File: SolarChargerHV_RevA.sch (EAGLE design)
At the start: 134 parts, among them CON1 CON_4X200MIL, CON2 USB_BMULTICOMP, CON3 ICSP, CON4 CON_3X100MIL, CON5 CON_3X100MIL, CON6 CON_8X200MIL, CON7 CON_2X100MIL, IC1 MCP3428, IC10 AT45DB161E, IC12 MCP14A0153, IC13 MCP14A0153, IC2 LMR62014, IC3 MIC4605-1YM, IC4 MCP1755, IC5 PIC18F46J50, IC6 TS6001, IC7 LMT86, IC8 24AA16, Q10 NTR4101PT1G, Q11 N-FET, Q12 N-FET, Q13 N-FET, Q14 N-FET, Q15 NX3008NBKW, Q2 PSMN6R0-30YL, Q3 NX3008NBKW, Q4 NTR4101PT1G, Q5 IPB039N10N3, Q6 IPB039N10N3, Q9 NX3008NBKW, X1 ABS07-120-32.768KHZ-T, X2 ABM3-8.000MHZ-D2Y-T, X3 USB_A, X4 USB_A

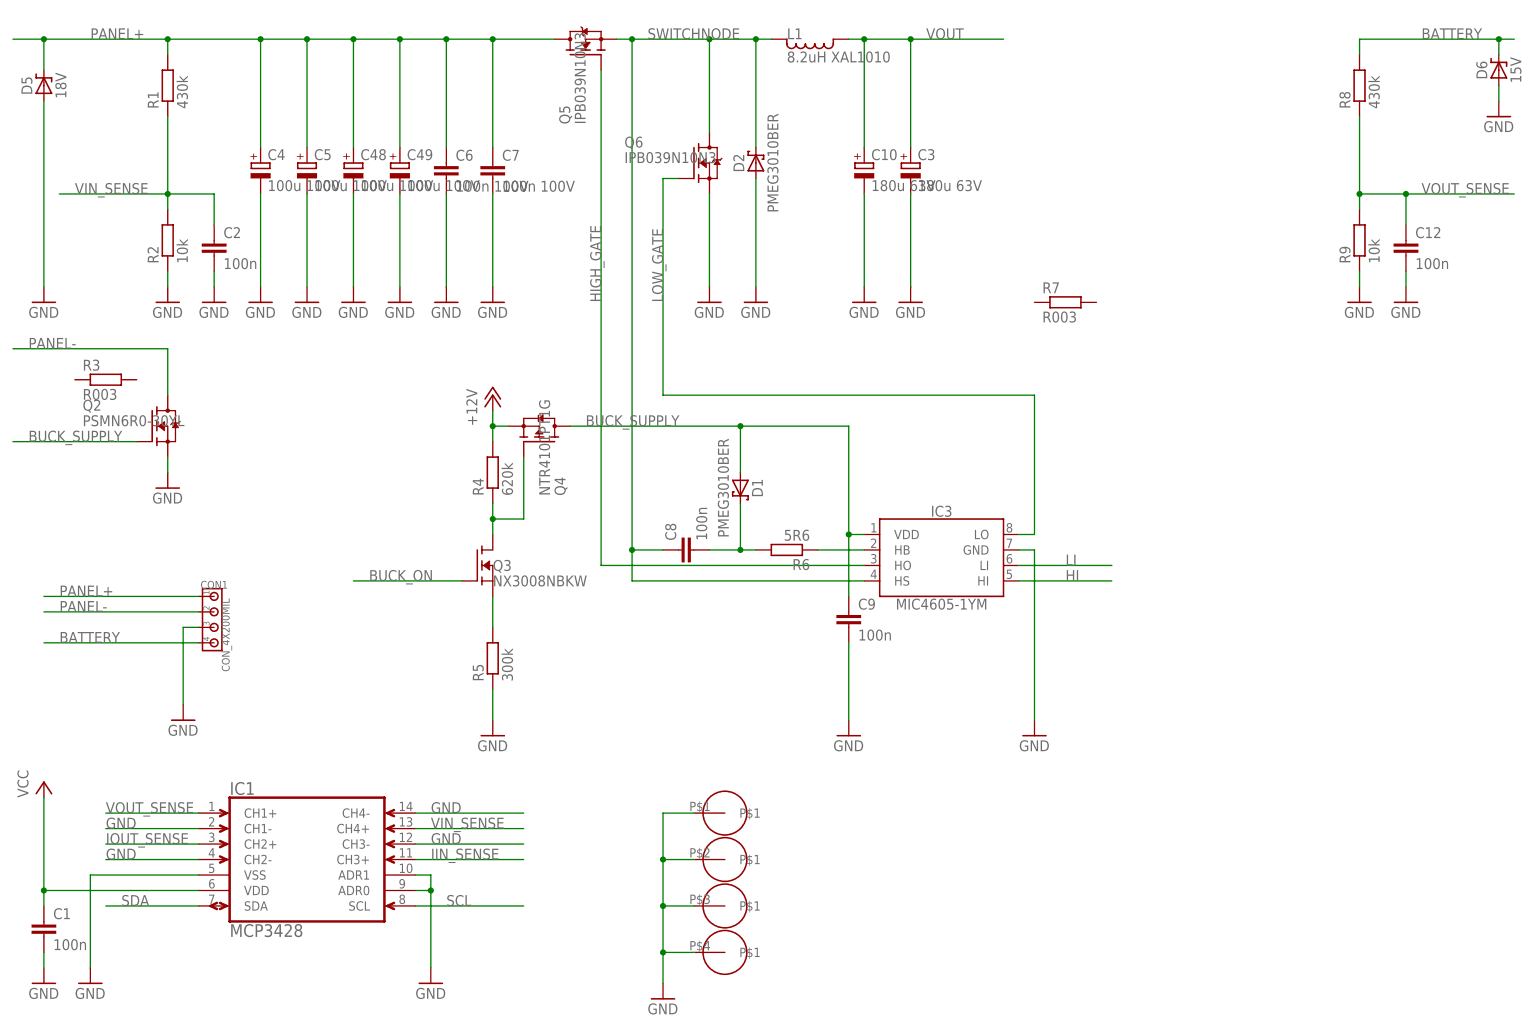
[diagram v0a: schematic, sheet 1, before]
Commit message: Buck for high voltage version nearly completed. Mosfet footprint still to be changed. Low-side current sensing implemented
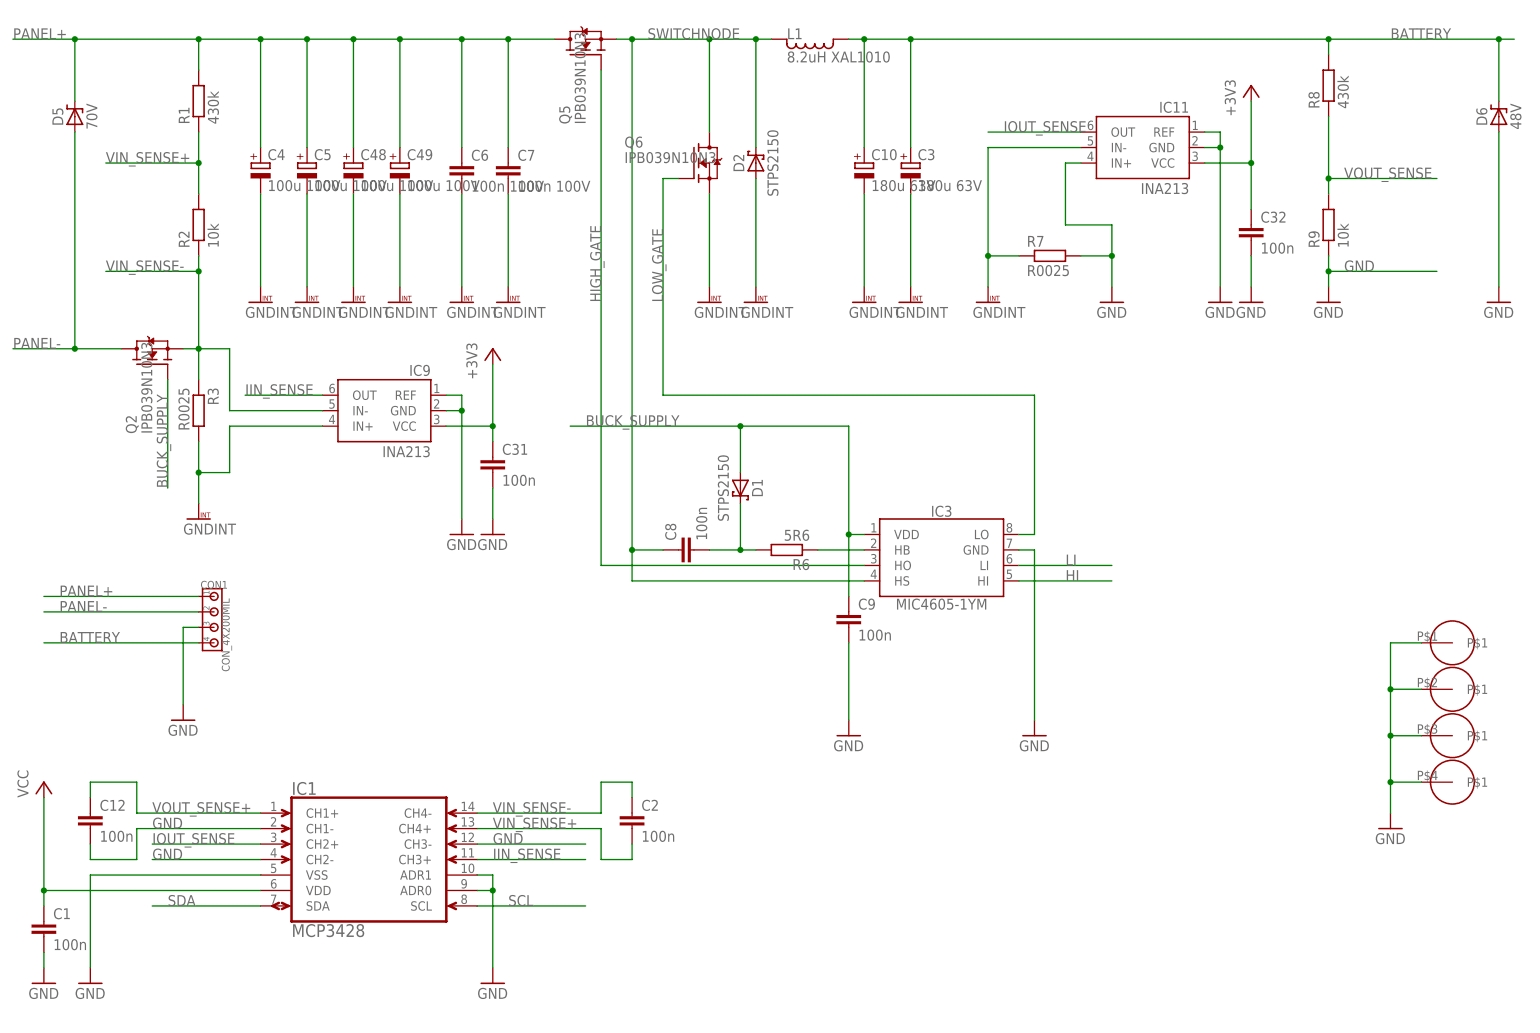
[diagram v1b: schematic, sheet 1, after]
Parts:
- removed Q3: NX3008NBKW, 00Mosfet:N-FETSOT23
- removed Q4: NTR4101PT1G, 00Mosfet:P-FETSOT23
- removed R4: 620k, 00Resistor:RESISTORR0805
- removed R5: 300k, 00Resistor:RESISTORR0805
- added C31, C32: 100n, 00Capacitor:CC0805
- added IC11, IC9: INA213, 00Sensor:INA21
- D1, D2: value PMEG3010BER -> STPS2150; device 00Diode:SCHOTTKYSOD123 -> 00Diode:SCHOTTKYDO214AC
- D5: value 18V -> 70V
- D6: value 15V -> 48V
- Q2: value PSMN6R0-30YL -> IPB039N10N3
- R3, R7: value R003 -> R0025
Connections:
- removed net N$16: Q3.D, Q4.G, R4.1
- removed net N$19: Q3.S, R5.2
- removed net VIN_SENSE: C2.1, IC1.CH4+, R1.1, R2.2
- removed net VOUT: C10.+, C3.+, L1.1, Q4.S, R4.2
- new net GNDINT: C10.-, C3.-, C4.-, C48.-, C49.-, C5.-, C6.2, C7.2, D2.A, IC11.IN-, IC9.IN+, Q6.S, R3.2, R7.1
- new net VIN_SENSE+: C2.2, IC1.CH4+, R1.1, R2.2
- new net VIN_SENSE-: C2.1, IC1.CH4-, IC9.IN-, Q2.S, R2.1, R3.1
- new net VOUT_SENSE+: C12.1, IC1.CH1+
- net +3V3: now also C31.1, C32.1, IC11.VCC, IC9.VCC
- net BATTERY: now also C10.+, C3.+, L1.1
- net BUCK_ON: no longer Q3.G
- net BUCK_SUPPLY: no longer Q4.D
- net GND: now also C31.2, C32.2, IC11.GND, IC11.IN+, IC11.REF, IC9.GND, IC9.REF, R7.2; no longer C10.-, C2.2, C3.-, C4.-, C48.-, C49.-, C5.-, C6.2, C7.2, D2.A, D5.A, IC1.CH4-, Q2.S, Q6.S, R2.1, R5.1
- net IIN_SENSE: now also IC9.OUT
- net IOUT_SENSE: now also IC11.OUT
- net PANEL-: now also D5.A
- net VOUT_SENSE: no longer C12.1, IC1.CH1+
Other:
- moved on the sheet: C12, C2, C6, C7, D5, D6, IC1, Q2, R1, R2, R3, R7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

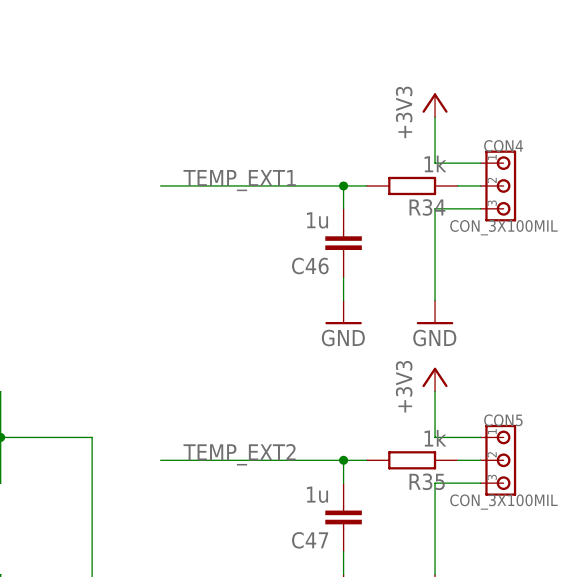
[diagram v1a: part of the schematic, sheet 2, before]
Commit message: Flash now supplied directly from VCC
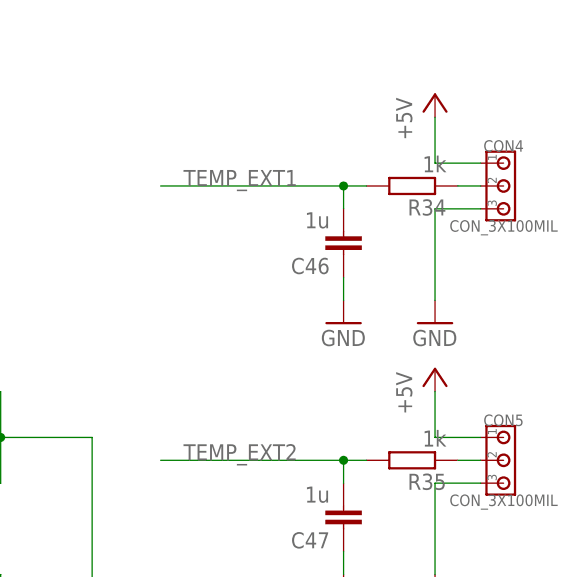
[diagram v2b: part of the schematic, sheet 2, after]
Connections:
- net +3V3: no longer CON4.1, CON5.1
- net +5V: now also CON4.1, CON5.1
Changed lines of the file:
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@@
 <part name="+3V2" library="00Supply" deviceset="+3V3" device=""/>
 <part name="+3V3" library="00Supply" deviceset="+3V3" device=""/>
-<part name="+3V4" library="00Supply" deviceset="+3V3" device=""/>
+<part name="+3V4" library="00Supply" deviceset="+5V" device=""/>
 <part name="+3V5" library="00Supply" deviceset="+3V3" device=""/>
 <part name="+3V6" library="00Supply" deviceset="+3V3" device=""/>
-<part name="+3V7" library="00Supply" deviceset="+3V3" device=""/>
+<part name="+3V7" library="00Supply" deviceset="+5V" device=""/>
 <part name="C31" library="00Capacitor" deviceset="C" device="C0805" value="100n"/>
 <part name="IC9" library="00Sensor" deviceset="INA21*" device="" value="INA213"/>
@@
 <instance part="+3V2" gate="G$1" x="127" y="33.02"/>
 <instance part="+3V3" gate="G$1" x="246.38" y="96.52"/>
-<instance part="+3V4" gate="G$1" x="238.76" y="167.64"/>
+<instance part="+3V4" gate="1" x="238.76" y="167.64"/>
 <instance part="+3V5" gate="G$1" x="104.14" y="170.18"/>
 <instance part="+3V6" gate="G$1" x="177.8" y="66.04"/>
-<instance part="+3V7" gate="G$1" x="238.76" y="137.16"/>
+<instance part="+3V7" gate="1" x="238.76" y="137.16"/>
 </instances>
 <busses>
@@
 </segment>
 <segment>
-<wire x1="238.76" y1="165.1" x2="238.76" y2="160.02" width="0.1524" layer="91"/>
-<pinref part="CON4" gate="G$1" pin="1"/>
-<wire x1="238.76" y1="160.02" x2="243.84" y2="160.02" width="0.1524" layer="91"/>
-<pinref part="+3V4" gate="G$1" pin="+3V3"/>
-</segment>
-<segment>
 <pinref part="C14" gate="G$1" pin="1"/>
 <pinref part="IC5" gate="G$1" pin="VUSB"/>
@@
 <pinref part="IC6" gate="G$1" pin="IN"/>
 <pinref part="+3V6" gate="G$1" pin="+3V3"/>
-</segment>
-<segment>
-<pinref part="CON5" gate="G$1" pin="1"/>
-<wire x1="243.84" y1="129.54" x2="238.76" y2="129.54" width="0.1524" layer="91"/>
-<wire x1="238.76" y1="129.54" x2="238.76" y2="134.62" width="0.1524" layer="91"/>
-<pinref part="+3V7" gate="G$1" pin="+3V3"/>
 </segment>
 </net>
@@
 </segment>
 </net>
+<net name="+5V" class="0">
+<segment>
+<wire x1="238.76" y1="165.1" x2="238.76" y2="160.02" width="0.1524" layer="91"/>
+<pinref part="CON4" gate="G$1" pin="1"/>
+<wire x1="238.76" y1="160.02" x2="243.84" y2="160.02" width="0.1524" layer="91"/>
+<pinref part="+3V4" gate="1" pin="+5V"/>
+</segment>
+<segment>
+<pinref part="CON5" gate="G$1" pin="1"/>
+<wire x1="243.84" y1="129.54" x2="238.76" y2="129.54" width="0.1524" layer="91"/>
+<wire x1="238.76" y1="129.54" x2="238.76" y2="134.62" width="0.1524" layer="91"/>
+<pinref part="+3V7" gate="1" pin="+5V"/>
+</segment>
+</net>
